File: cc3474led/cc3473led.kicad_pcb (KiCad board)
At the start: 2 copper layers, 76.2 x 71.1 mm, 42 parts, among them IC1 LT3474, P1 PWM, P2 CONN_01X02, P3 CONN_01X10, P4 CONN_01X10, P5 CONN_01X02, Q1 IRLM0060, U1 MCP16331

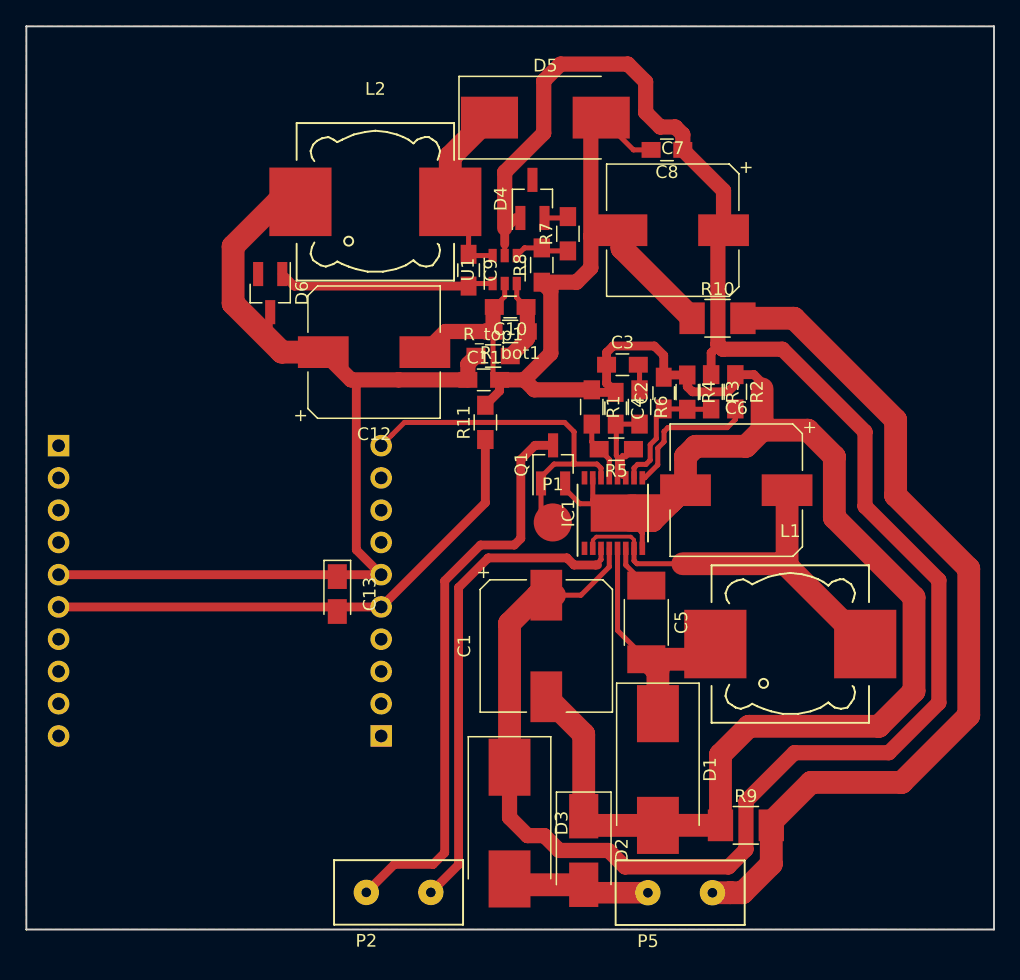
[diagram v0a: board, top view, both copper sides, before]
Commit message: changed resistor values
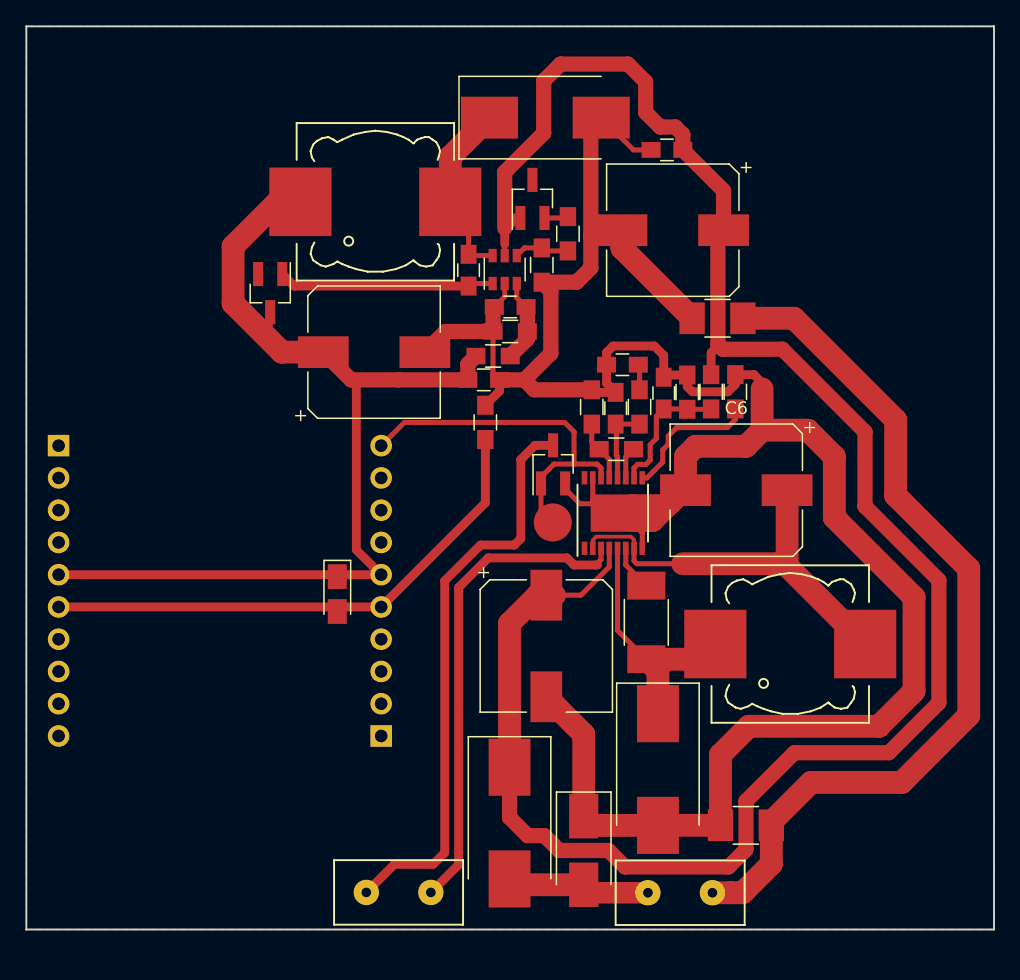
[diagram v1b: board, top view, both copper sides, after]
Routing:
- net Net-(IC1-Pad11): track 0.85 -> 2.50 mm
- net (no net): track 1.65 -> 0.00 mm

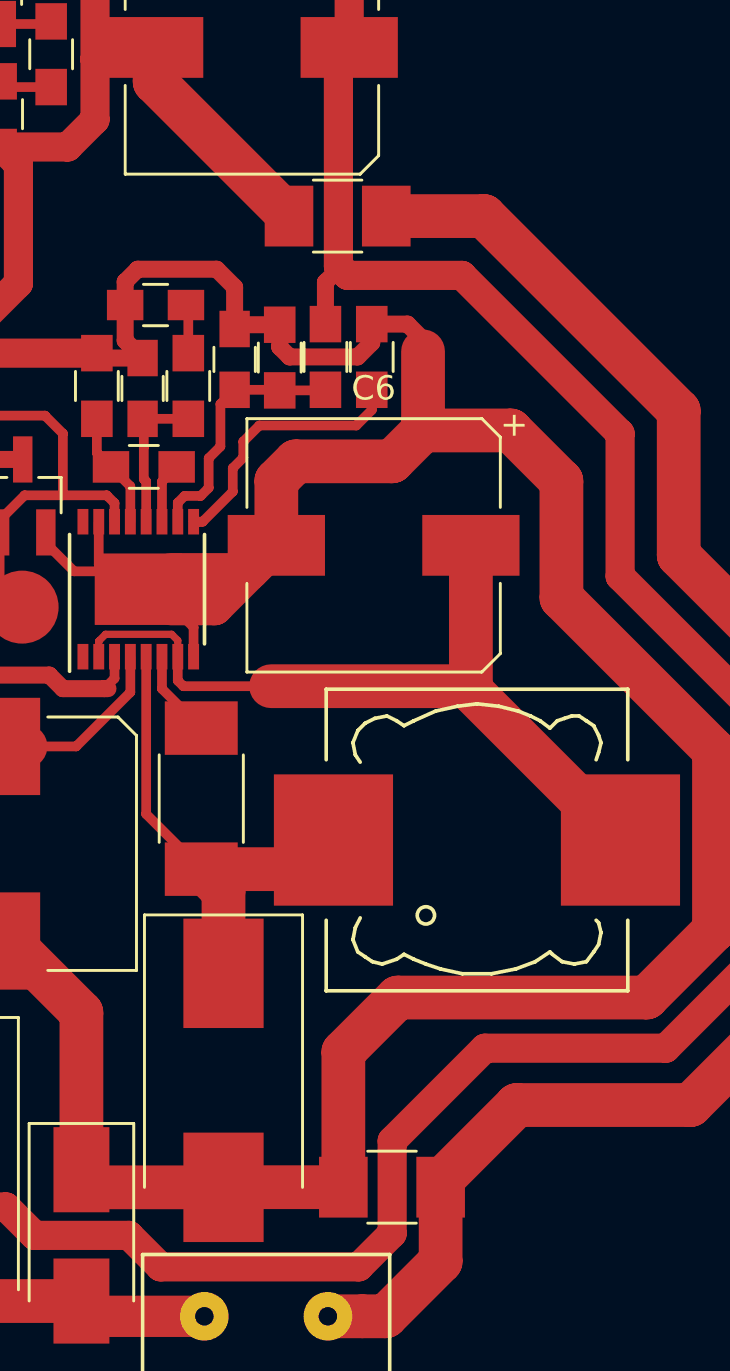
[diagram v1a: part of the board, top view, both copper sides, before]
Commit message: changed size of 0R resistors
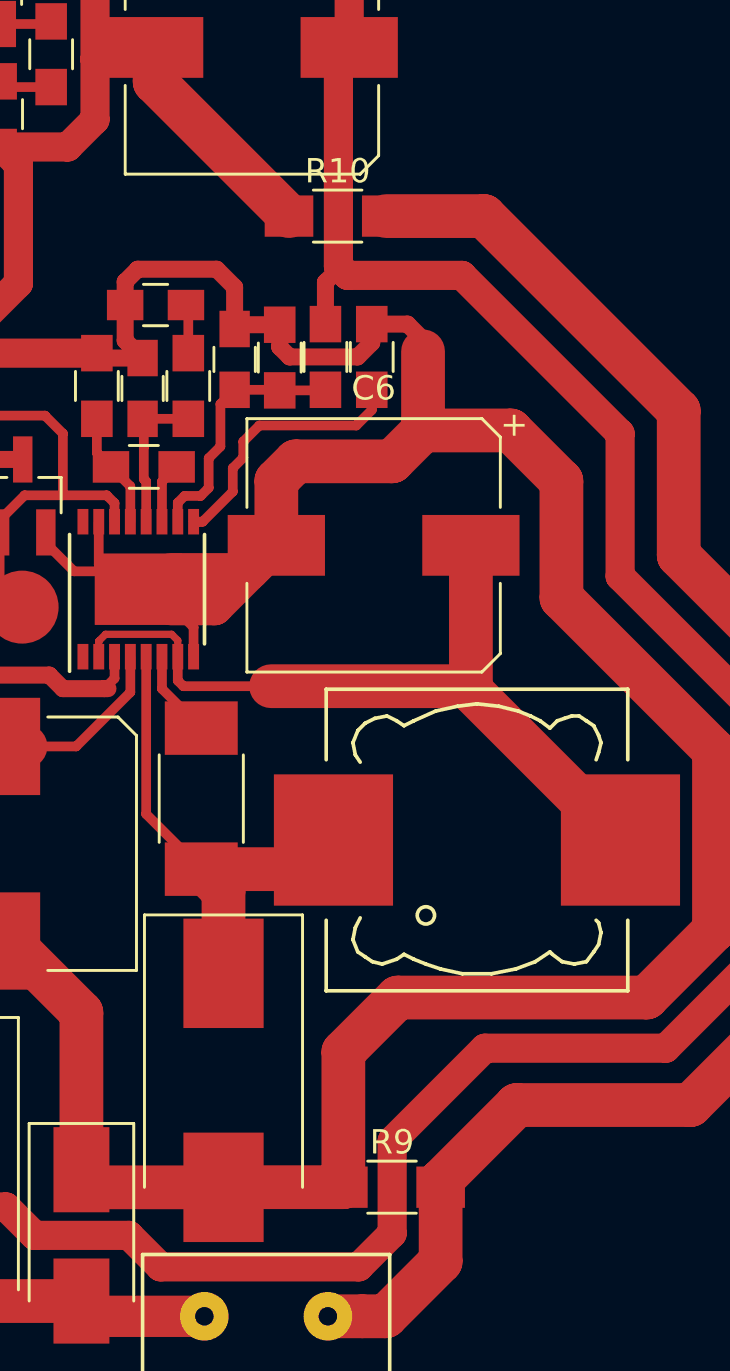
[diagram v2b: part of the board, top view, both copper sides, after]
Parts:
- R10, R9: footprint Resistors_SMD:R_1210_HandSoldering -> Resistors_SMD:R_1206_HandSoldering
- R2: value 80k6 -> 82k
- R4: value 28k3 -> 27k
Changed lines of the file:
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@@
   (general
     (links 88)
-    (no_connects 2)
-    (area 132.126667 58.344999 226.29 139.860001)
+    (no_connects 1)
+    (area 134.544999 58.344999 210.895001 129.615001)
     (thickness 1.6)
     (drawings 6)
@@
       (effects (font (size 1 1) (thickness 0.15)))
     )
-    (fp_text value 80k6 (at 0 -0.8128 270) (layer F.Fab) hide
+    (fp_text value 82k (at 0 -0.8128 270) (layer F.Fab) hide
       (effects (font (size 1 1) (thickness 0.15)))
     )
@@
       (effects (font (size 1 1) (thickness 0.15)))
     )
-    (fp_text value 28k3 (at 0 1.75 270) (layer F.Fab) hide
+    (fp_text value 27k (at 0 1.75 270) (layer F.Fab) hide
       (effects (font (size 1 1) (thickness 0.15)))
     )
@@
       (net 13 "/Power Protection/V_IN"))
   )
-  (module Resistors_SMD:R_1210_HandSoldering (layer F.Cu)
-    (at 191.2808 121.3358)
-    (descr "Resistor SMD 1210, hand soldering")
-    (tags "resistor 1210")
-    (attr smd)
-    (fp_text reference R9 (at 0 -2.3) (layer F.SilkS) hide
-      (effects (font (size 1 1) (thickness 0.15)))
-    )
-    (fp_text value 0R (at -0.0188 0.0762 90) (layer F.Fab) hide
-      (effects (font (size 1 1) (thickness 0.15)))
-    )
-    (fp_text user %R (at -0.0188 0 90) (layer F.Fab)
-      (effects (font (size 0.7 0.7) (thickness 0.105)))
-    )
-    (fp_line (start -1.6 1.25) (end -1.6 -1.25) (layer F.Fab) (width 0.1))
-    (fp_line (start 1.6 1.25) (end -1.6 1.25) (layer F.Fab) (width 0.1))
-    (fp_line (start 1.6 -1.25) (end 1.6 1.25) (layer F.Fab) (width 0.1))
-    (fp_line (start -1.6 -1.25) (end 1.6 -1.25) (layer F.Fab) (width 0.1))
-    (fp_line (start 1 1.48) (end -1 1.48) (layer F.SilkS) (width 0.12))
-    (fp_line (start -1 -1.48) (end 1 -1.48) (layer F.SilkS) (width 0.12))
-    (fp_line (start -3.25 -1.5) (end 3.25 -1.5) (layer F.CrtYd) (width 0.05))
-    (fp_line (start -3.25 -1.5) (end -3.25 1.5) (layer F.CrtYd) (width 0.05))
-    (fp_line (start 3.25 1.5) (end 3.25 -1.5) (layer F.CrtYd) (width 0.05))
-    (fp_line (start 3.25 1.5) (end -3.25 1.5) (layer F.CrtYd) (width 0.05))
-    (pad 1 smd rect (at -2 0) (size 2 2.5) (layers F.Cu F.Paste F.Mask)
-      (net 2 GND))
-    (pad 2 smd rect (at 2 0) (size 2 2.5) (layers F.Cu F.Paste F.Mask)
-      (net 2 GND))
-    (model ${KISYS3DMOD}/Resistors_SMD.3dshapes/R_1210.wrl
-      (at (xyz 0 0 0))
-      (scale (xyz 1 1 1))
-      (rotate (xyz 0 0 0))
-    )
-  )
-  (module Resistors_SMD:R_1210_HandSoldering (layer F.Cu)
-    (at 189.0456 81.407)
-    (descr "Resistor SMD 1210, hand soldering")
-    (tags "resistor 1210")
-    (attr smd)
-    (fp_text reference R10 (at 0 -2.3) (layer F.SilkS) hide
-      (effects (font (size 1 1) (thickness 0.15)))
-    )
-    (fp_text value 0R (at 0 2.4) (layer F.Fab) hide
-      (effects (font (size 1 1) (thickness 0.15)))
-    )
-    (fp_text user %R (at 0 0 90) (layer F.Fab)
-      (effects (font (size 0.7 0.7) (thickness 0.105)))
-    )
-    (fp_line (start -1.6 1.25) (end -1.6 -1.25) (layer F.Fab) (width 0.1))
-    (fp_line (start 1.6 1.25) (end -1.6 1.25) (layer F.Fab) (width 0.1))
-    (fp_line (start 1.6 -1.25) (end 1.6 1.25) (layer F.Fab) (width 0.1))
-    (fp_line (start -1.6 -1.25) (end 1.6 -1.25) (layer F.Fab) (width 0.1))
-    (fp_line (start 1 1.48) (end -1 1.48) (layer F.SilkS) (width 0.12))
-    (fp_line (start -1 -1.48) (end 1 -1.48) (layer F.SilkS) (width 0.12))
-    (fp_line (start -3.25 -1.5) (end 3.25 -1.5) (layer F.CrtYd) (width 0.05))
-    (fp_line (start -3.25 -1.5) (end -3.25 1.5) (layer F.CrtYd) (width 0.05))
-    (fp_line (start 3.25 1.5) (end 3.25 -1.5) (layer F.CrtYd) (width 0.05))
-    (fp_line (start 3.25 1.5) (end -3.25 1.5) (layer F.CrtYd) (width 0.05))
-    (pad 1 smd rect (at -2 0) (size 2 2.5) (layers F.Cu F.Paste F.Mask)
-      (net 2 GND))
-    (pad 2 smd rect (at 2 0) (size 2 2.5) (layers F.Cu F.Paste F.Mask)
-      (net 2 GND))
-    (model ${KISYS3DMOD}/Resistors_SMD.3dshapes/R_1210.wrl
-      (at (xyz 0 0 0))
-      (scale (xyz 1 1 1))
-      (rotate (xyz 0 0 0))
-    )
-  )
   (module Capacitors_Tantalum_SMD:CP_Tantalum_Case-A_EIA-3216-18_Reflow (layer F.Cu)
     (at 159.1056 103.124 270)
@@
       (at (xyz 0 0 0))
       (scale (xyz 1 1 1))
+      (rotate (xyz 0 0 0))
+    )
+  )
+  (module Resistors_SMD:R_1206_HandSoldering (layer F.Cu)
+    (at 191.2808 121.3358)
+    (descr "Resistor SMD 1206, hand soldering")
+    (tags "resistor 1206")
+    (attr smd)
+    (fp_text reference R9 (at 0 -1.85) (layer F.SilkS)
+      (effects (font (size 1 1) (thickness 0.15)))
+    )
+    (fp_text value 0R (at 0 1.9) (layer F.Fab)
+      (effects (font (size 1 1) (thickness 0.15)))
+    )
+    (fp_text user %R (at 0 0) (layer F.Fab)
+      (effects (font (size 0.7 0.7) (thickness 0.105)))
+    )
+    (fp_line (start -1.6 0.8) (end -1.6 -0.8) (layer F.Fab) (width 0.1))
+    (fp_line (start 1.6 0.8) (end -1.6 0.8) (layer F.Fab) (width 0.1))
+    (fp_line (start 1.6 -0.8) (end 1.6 0.8) (layer F.Fab) (width 0.1))
+    (fp_line (start -1.6 -0.8) (end 1.6 -0.8) (layer F.Fab) (width 0.1))
+    (fp_line (start 1 1.07) (end -1 1.07) (layer F.SilkS) (width 0.12))
+    (fp_line (start -1 -1.07) (end 1 -1.07) (layer F.SilkS) (width 0.12))
+    (fp_line (start -3.25 -1.11) (end 3.25 -1.11) (layer F.CrtYd) (width 0.05))
+    (fp_line (start -3.25 -1.11) (end -3.25 1.1) (layer F.CrtYd) (width 0.05))
+    (fp_line (start 3.25 1.1) (end 3.25 -1.11) (layer F.CrtYd) (width 0.05))
+    (fp_line (start 3.25 1.1) (end -3.25 1.1) (layer F.CrtYd) (width 0.05))
+    (pad 1 smd rect (at -2 0) (size 2 1.7) (layers F.Cu F.Paste F.Mask)
+      (net 2 GND))
+    (pad 2 smd rect (at 2 0) (size 2 1.7) (layers F.Cu F.Paste F.Mask)
+      (net 2 GND))
+    (model ${KISYS3DMOD}/Resistors_SMD.3dshapes/R_1206.wrl
+      (at (xyz 0 0 0))
+      (scale (xyz 1 1 1))
+      (rotate (xyz 0 0 0))
+    )
+  )
+  (module Resistors_SMD:R_1206_HandSoldering (layer F.Cu)
+    (at 189.0456 81.407)
+    (descr "Resistor SMD 1206, hand soldering")
+    (tags "resistor 1206")
+    (attr smd)
+    (fp_text reference R10 (at 0 -1.85) (layer F.SilkS)
+      (effects (font (size 1 1) (thickness 0.15)))
+    )
+    (fp_text value 0R (at 0 1.9) (layer F.Fab)
+      (effects (font (size 1 1) (thickness 0.15)))
+    )
+    (fp_text user %R (at 0 0) (layer F.Fab)
+      (effects (font (size 0.7 0.7) (thickness 0.105)))
+    )
+    (fp_line (start -1.6 0.8) (end -1.6 -0.8) (layer F.Fab) (width 0.1))
+    (fp_line (start 1.6 0.8) (end -1.6 0.8) (layer F.Fab) (width 0.1))
+    (fp_line (start 1.6 -0.8) (end 1.6 0.8) (layer F.Fab) (width 0.1))
+    (fp_line (start -1.6 -0.8) (end 1.6 -0.8) (layer F.Fab) (width 0.1))
+    (fp_line (start 1 1.07) (end -1 1.07) (layer F.SilkS) (width 0.12))
+    (fp_line (start -1 -1.07) (end 1 -1.07) (layer F.SilkS) (width 0.12))
+    (fp_line (start -3.25 -1.11) (end 3.25 -1.11) (layer F.CrtYd) (width 0.05))
+    (fp_line (start -3.25 -1.11) (end -3.25 1.1) (layer F.CrtYd) (width 0.05))
+    (fp_line (start 3.25 1.1) (end 3.25 -1.11) (layer F.CrtYd) (width 0.05))
+    (fp_line (start 3.25 1.1) (end -3.25 1.1) (layer F.CrtYd) (width 0.05))
+    (pad 1 smd rect (at -2 0) (size 2 1.7) (layers F.Cu F.Paste F.Mask)
+      (net 2 GND))
+    (pad 2 smd rect (at 2 0) (size 2 1.7) (layers F.Cu F.Paste F.Mask)
+      (net 2 GND))
+    (model ${KISYS3DMOD}/Resistors_SMD.3dshapes/R_1206.wrl
+      (at (xyz 0 0 0))
+      (scale (xyz 1 1 1))
